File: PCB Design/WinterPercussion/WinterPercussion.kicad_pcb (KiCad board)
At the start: 2 copper layers, 55.9 x 59 mm, 7 parts, among them J1 SDS-50J, U1 6N138, U2 ESP32-DevKitC

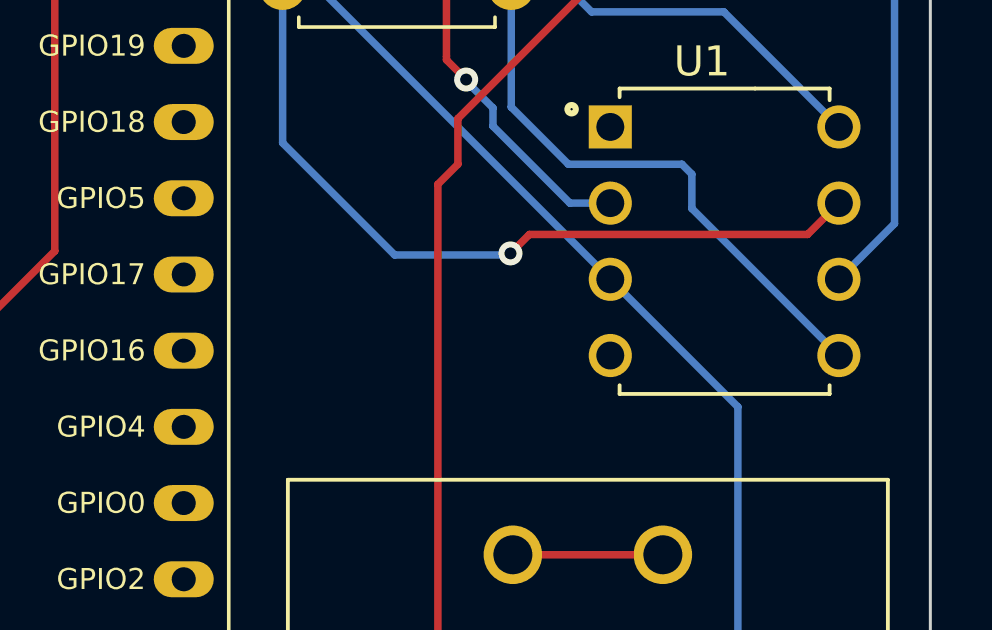
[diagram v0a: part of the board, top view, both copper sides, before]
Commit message: Updated with Pin16 from Mark
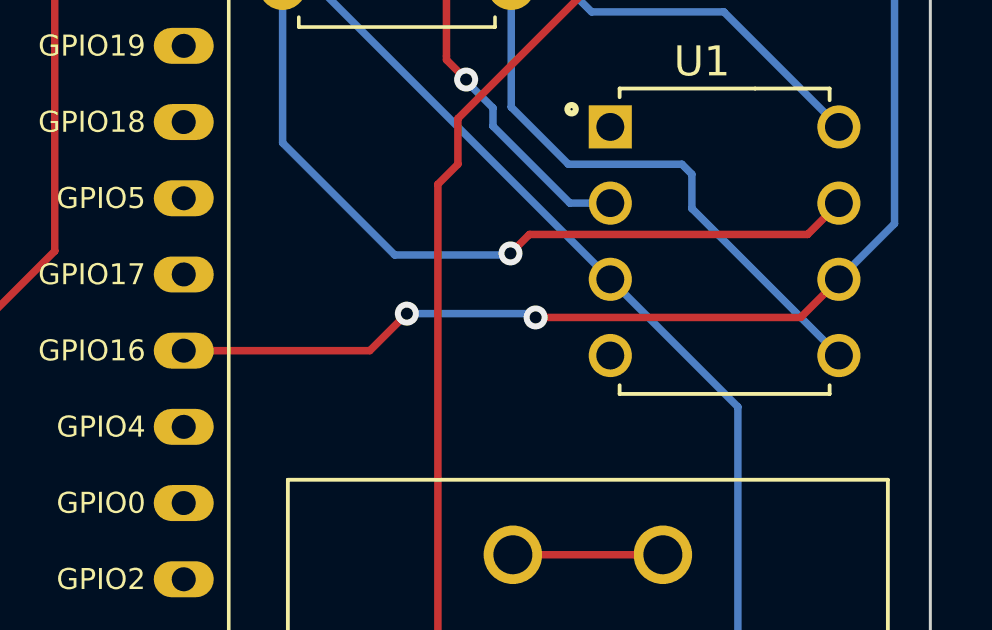
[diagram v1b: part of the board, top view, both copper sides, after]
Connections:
- U2 pad 27: unconnected-(U2-Pad27) -> ESP_PIN
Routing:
- net ESP_PIN: track 28.5 -> 51.4 mm, vias 0 -> 2
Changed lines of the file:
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@@
   (net 35 "unconnected-(U2-Pad25)")
   (net 36 "unconnected-(U2-Pad26)")
-  (net 37 "unconnected-(U2-Pad27)")
-  (net 38 "unconnected-(U2-Pad28)")
-  (net 39 "unconnected-(U2-Pad29)")
-  (net 40 "unconnected-(U2-Pad30)")
-  (net 41 "unconnected-(U2-Pad31)")
-  (net 42 "unconnected-(U2-Pad32)")
-  (net 43 "unconnected-(U2-Pad33)")
-  (net 44 "unconnected-(U2-Pad34)")
-  (net 45 "unconnected-(U2-Pad35)")
-  (net 46 "unconnected-(U2-Pad36)")
-  (net 47 "unconnected-(U2-Pad37)")
-  (net 48 "unconnected-(U1-Pad1)")
-  (net 49 "unconnected-(U1-Pad4)")
+  (net 37 "unconnected-(U2-Pad28)")
+  (net 38 "unconnected-(U2-Pad29)")
+  (net 39 "unconnected-(U2-Pad30)")
+  (net 40 "unconnected-(U2-Pad31)")
+  (net 41 "unconnected-(U2-Pad32)")
+  (net 42 "unconnected-(U2-Pad33)")
+  (net 43 "unconnected-(U2-Pad34)")
+  (net 44 "unconnected-(U2-Pad35)")
+  (net 45 "unconnected-(U2-Pad36)")
+  (net 46 "unconnected-(U2-Pad37)")
+  (net 47 "unconnected-(U1-Pad1)")
+  (net 48 "unconnected-(U1-Pad4)")
   (footprint "Connector_Audio:CUI_SDS-50J" (layer "F.Cu")
     (at 146.1151 100.592 180)
@@
     (property "Sheetname" "")
     (attr through_hole)
-    (fp_text reference "J1" (at -6.825 -9.635) (layer "F.SilkS")
-      (effects (font (size 1 1) (thickness 0.15)))
-    )
-    (fp_text value "SDS-50J" (at -3.015 8.635) (layer "F.Fab")
-      (effects (font (size 1 1) (thickness 0.15)))
-    )
+    (fp_text reference "J1" (at -6.825 -9.635 180) (layer "F.SilkS")
+      (effects (font (size 1 1) (thickness 0.15)))
+    )
+    (fp_text value "SDS-50J" (at -3.015 8.635 180) (layer "F.Fab")
+      (effects (font (size 1 1) (thickness 0.15)))
+    )
+    (fp_line (start -10 7.5) (end 10 7.5) (layer "F.SilkS") (width 0.127))
     (fp_line (start -10 7.5) (end -10 -8.3) (layer "F.SilkS") (width 0.127))
+    (fp_line (start 10 -8.3) (end 10 7.5) (layer "F.SilkS") (width 0.127))
+    (fp_line (start -10 -8.3) (end -6.5 -8.3) (layer "F.SilkS") (width 0.127))
     (fp_line (start 6.5 -8.3) (end 10 -8.3) (layer "F.SilkS") (width 0.127))
-    (fp_line (start -10 7.5) (end 10 7.5) (layer "F.SilkS") (width 0.127))
-    (fp_line (start -10 -8.3) (end -6.5 -8.3) (layer "F.SilkS") (width 0.127))
-    (fp_line (start 10 -8.3) (end 10 7.5) (layer "F.SilkS") (width 0.127))
     (fp_circle (center 10.764 -5.094) (end 10.864 -5.094) (layer "F.SilkS") (width 0.2) (fill none))
+    (fp_line (start 10.25 -8.55) (end 10.25 7.75) (layer "F.CrtYd") (width 0.05))
+    (fp_line (start -10.25 -8.55) (end -6.25 -8.55) (layer "F.CrtYd") (width 0.05))
     (fp_line (start 10.25 7.75) (end -10.25 7.75) (layer "F.CrtYd") (width 0.05))
+    (fp_line (start -6.25 -8.55) (end -6.25 -8.75) (layer "F.CrtYd") (width 0.05))
+    (fp_line (start -10.25 7.75) (end -10.25 -8.55) (layer "F.CrtYd") (width 0.05))
     (fp_line (start -6.25 -8.75) (end 6.25 -8.75) (layer "F.CrtYd") (width 0.05))
     (fp_line (start 6.25 -8.55) (end 10.25 -8.55) (layer "F.CrtYd") (width 0.05))
-    (fp_line (start 10.25 -8.55) (end 10.25 7.75) (layer "F.CrtYd") (width 0.05))
-    (fp_line (start -10.25 -8.55) (end -6.25 -8.55) (layer "F.CrtYd") (width 0.05))
     (fp_line (start 6.25 -8.75) (end 6.25 -8.55) (layer "F.CrtYd") (width 0.05))
-    (fp_line (start -10.25 7.75) (end -10.25 -8.55) (layer "F.CrtYd") (width 0.05))
-    (fp_line (start -6.25 -8.55) (end -6.25 -8.75) (layer "F.CrtYd") (width 0.05))
     (fp_line (start 10 -8.3) (end 10 7.5) (layer "F.Fab") (width 0.127))
+    (fp_line (start -10 7.5) (end -10 -8.3) (layer "F.Fab") (width 0.127))
     (fp_line (start -10 -8.3) (end 10 -8.3) (layer "F.Fab") (width 0.127))
-    (fp_line (start -10 7.5) (end -10 -8.3) (layer "F.Fab") (width 0.127))
     (fp_line (start 10 7.5) (end -10 7.5) (layer "F.Fab") (width 0.127))
     (fp_circle (center 10.764 -5.094) (end 10.864 -5.094) (layer "F.Fab") (width 0.2) (fill none))
@@
     (fp_line (start -3.5 -5.09) (end 3.5 -5.09) (layer "F.Fab") (width 0.127))
     (pad "1" thru_hole rect locked (at -3.81 -3.81) (size 1.438 1.438) (drill 0.93) (layers *.Cu *.Mask)
-      (net 48 "unconnected-(U1-Pad1)") (pinfunction "NC") (pintype "no_connect"))
+      (net 47 "unconnected-(U1-Pad1)") (pinfunction "NC") (pintype "no_connect"))
     (pad "2" thru_hole circle locked (at -3.81 -1.27) (size 1.438 1.438) (drill 0.93) (layers *.Cu *.Mask)
       (net 2 "Net-(D1-Pad2)") (pinfunction "C1") (pintype "passive"))
@@
       (net 1 "Net-(D1-Pad1)") (pinfunction "C2") (pintype "passive"))
     (pad "4" thru_hole circle locked (at -3.81 3.81) (size 1.438 1.438) (drill 0.93) (layers *.Cu *.Mask)
-      (net 49 "unconnected-(U1-Pad4)") (pinfunction "NC") (pintype "no_connect"))
+      (net 48 "unconnected-(U1-Pad4)") (pinfunction "NC") (pintype "no_connect"))
     (pad "5" thru_hole circle locked (at 3.81 3.81) (size 1.438 1.438) (drill 0.93) (layers *.Cu *.Mask)
       (net 9 "GND") (pinfunction "GND") (pintype "passive"))
@@
       (net 36 "unconnected-(U2-Pad26)") (pinfunction "ADC2_CH0/GPIO4") (pintype "bidirectional+no_connect"))
     (pad "27" thru_hole oval (at 25.40368 27.94272 270) (size 1.2 2) (drill 0.8) (layers *.Cu *.Mask)
-      (net 37 "unconnected-(U2-Pad27)") (pinfunction "GPIO16") (pintype "bidirectional+no_connect"))
+      (net 11 "ESP_PIN") (pinfunction "GPIO16") (pintype "bidirectional"))
     (pad "28" thru_hole oval (at 25.40368 25.40272 270) (size 1.2 2) (drill 0.8) (layers *.Cu *.Mask)
-      (net 38 "unconnected-(U2-Pad28)") (pinfunction "GPIO17") (pintype "bidirectional+no_connect"))
+      (net 37 "unconnected-(U2-Pad28)") (pinfunction "GPIO17") (pintype "bidirectional+no_connect"))
     (pad "29" thru_hole oval (at 25.40368 22.86272 270) (size 1.2 2) (drill 0.8) (layers *.Cu *.Mask)
-      (net 39 "unconnected-(U2-Pad29)") (pinfunction "*GPIO5") (pintype "bidirectional+no_connect"))
+      (net 38 "unconnected-(U2-Pad29)") (pinfunction "*GPIO5") (pintype "bidirectional+no_connect"))
     (pad "30" thru_hole oval (at 25.40368 20.32272 270) (size 1.2 2) (drill 0.8) (layers *.Cu *.Mask)
-      (net 40 "unconnected-(U2-Pad30)") (pinfunction "GPIO18") (pintype "bidirectional+no_connect"))
+      (net 39 "unconnected-(U2-Pad30)") (pinfunction "GPIO18") (pintype "bidirectional+no_connect"))
     (pad "31" thru_hole oval (at 25.40368 17.78272 270) (size 1.2 2) (drill 0.8) (layers *.Cu *.Mask)
-      (net 41 "unconnected-(U2-Pad31)") (pinfunction "GPIO19") (pintype "bidirectional+no_connect"))
+      (net 40 "unconnected-(U2-Pad31)") (pinfunction "GPIO19") (pintype "bidirectional+no_connect"))
     (pad "32" thru_hole oval (at 25.40368 15.24272 270) (size 1.2 2) (drill 0.8) (layers *.Cu *.Mask)
-      (net 42 "unconnected-(U2-Pad32)") (pinfunction "GND") (pintype "power_in+no_connect"))
+      (net 41 "unconnected-(U2-Pad32)") (pinfunction "GND") (pintype "power_in+no_connect"))
     (pad "33" thru_hole oval (at 25.40368 12.70272 270) (size 1.2 2) (drill 0.8) (layers *.Cu *.Mask)
-      (net 43 "unconnected-(U2-Pad33)") (pinfunction "GPIO21") (pintype "bidirectional+no_connect"))
+      (net 42 "unconnected-(U2-Pad33)") (pinfunction "GPIO21") (pintype "bidirectional+no_connect"))
     (pad "34" thru_hole oval (at 25.40368 10.16272 270) (size 1.2 2) (drill 0.8) (layers *.Cu *.Mask)
-      (net 44 "unconnected-(U2-Pad34)") (pinfunction "U0RXD/GPIO3") (pintype "bidirectional+no_connect"))
+      (net 43 "unconnected-(U2-Pad34)") (pinfunction "U0RXD/GPIO3") (pintype "bidirectional+no_connect"))
     (pad "35" thru_hole oval (at 25.40368 7.62272 270) (size 1.2 2) (drill 0.8) (layers *.Cu *.Mask)
-      (net 45 "unconnected-(U2-Pad35)") (pinfunction "U0TXD/GPIO1") (pintype "bidirectional+no_connect"))
+      (net 44 "unconnected-(U2-Pad35)") (pinfunction "U0TXD/GPIO1") (pintype "bidirectional+no_connect"))
     (pad "36" thru_hole oval (at 25.40368 5.08272 270) (size 1.2 2) (drill 0.8) (layers *.Cu *.Mask)
-      (net 46 "unconnected-(U2-Pad36)") (pinfunction "GPIO22") (pintype "bidirectional+no_connect"))
+      (net 45 "unconnected-(U2-Pad36)") (pinfunction "GPIO22") (pintype "bidirectional+no_connect"))
     (pad "37" thru_hole oval (at 25.40368 2.54272 270) (size 1.2 2) (drill 0.8) (layers *.Cu *.Mask)
-      (net 47 "unconnected-(U2-Pad37)") (pinfunction "GPIO23") (pintype "bidirectional+no_connect"))
+      (net 46 "unconnected-(U2-Pad37)") (pinfunction "GPIO23") (pintype "bidirectional+no_connect"))
     (pad "38" thru_hole roundrect (at 25.40368 0.00272 270) (size 1.2 2) (drill 0.8) (layers *.Cu *.Mask) (roundrect_rratio 0.25)
       (net 9 "GND") (pinfunction "GND") (pintype "power_in"))
@@
   (segment (start 136.21901 67.47617) (end 146.23824 77.4954) (width 0.25) (layer "B.Cu") (net 10))
   (segment (start 146.23824 77.4954) (end 150.6474 77.4954) (width 0.25) (layer "B.Cu") (net 10))
+  (segment (start 144.3736 87.6808) (end 153.2128 87.6808) (width 0.25) (layer "F.Cu") (net 11))
+  (segment (start 132.6444 88.78892) (end 138.84588 88.78892) (width 0.25) (layer "F.Cu") (net 11))
+  (segment (start 153.2128 87.6808) (end 154.4828 86.4108) (width 0.25) (layer "F.Cu") (net 11))
+  (segment (start 138.84588 88.78892) (end 140.081 87.5538) (width 0.25) (layer "F.Cu") (net 11))
+  (via (at 144.3736 87.6808) (size 0.8) (drill 0.4) (layers "F.Cu" "B.Cu") (net 11))
+  (via (at 140.081 87.5538) (size 0.8) (drill 0.4) (layers "F.Cu" "B.Cu") (net 11))
   (segment (start 156.337 84.5566) (end 154.4828 86.4108) (width 0.25) (layer "B.Cu") (net 11))
   (segment (start 148.0058 66.3448) (end 156.337 74.676) (width 0.25) (layer "B.Cu") (net 11))
   (segment (start 156.337 74.676) (end 156.337 84.5566) (width 0.25) (layer "B.Cu") (net 11))
+  (segment (start 144.2466 87.5538) (end 144.3736 87.6808) (width 0.25) (layer "B.Cu") (net 11))
   (segment (start 143.83901 66.3448) (end 148.0058 66.3448) (width 0.25) (layer "B.Cu") (net 11))
+  (segment (start 140.081 87.5538) (end 144.2466 87.5538) (width 0.25) (layer "B.Cu") (net 11))
 )

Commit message: Updated KiCad Docs
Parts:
- removed R3: 470Ω, Resistor_THT:R_Axial_DIN0207_L6.3mm_D2.5mm_P7.62mm_Horizontal
- R2: value 10kΩ -> 270Ω
- U1: value 6N138 -> H11L1M; footprint OptoCoupler:DIP762W50P254L1018H450Q8 -> Opto:H11L1M
- moved U1 10.7 mm to (140.5, 82.1)
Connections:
- R2 pad 1: Net-(R2-Pad1) -> +5V
- R2 pad 2: GND -> ESP_PIN
- U1 pad 1: unconnected-(U1-Pad1) -> Net-(D1-Pad2)
- U1 pad 2: Net-(D1-Pad2) -> Net-(D1-Pad1)
- U1 pad 3: Net-(D1-Pad1) -> unconnected-(U1-Pad3)
- U1 pad 4: unconnected-(U1-Pad4) -> ESP_PIN
- U1 pad 6: ESP_PIN -> +5V
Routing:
- net Net-(R2-Pad1): track 26.0 -> 0.00 mm, vias 1 -> 0
- net ESP_PIN: track 51.4 -> 28.0 mm, vias 2 -> 0
- net +5V: track 81.5 -> 67.2 mm, vias 0 -> 2
- net Net-(D1-Pad1): track 42.7 -> 47.2 mm, vias 0 -> 1
- net Net-(D1-Pad2): track 29.0 -> 25.8 mm, vias 2 -> 0
- net Net-(J1-Pad4): track 51.5 -> 49.3 mm
- net GND: track 47.6 -> 46.7 mm
